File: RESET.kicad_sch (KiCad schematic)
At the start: 14 parts

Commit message: changed bus names to avoid possible conflicts, fixed unnamed busses.
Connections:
- net PABO_{2}_{3}: now reaches U?.12 (Zd)
- net PABO_{2}_{0}: now reaches U?.4 (Za)
- net PABO_{2}_{1}: now reaches U?.7 (Zb)
- net PABO_{2}_{2}: now reaches U?.9 (Zc)
- net PABO_{4}_{3}: now reaches U?.12 (Zd)
- net PABO_{4}_{0}: now reaches U?.4 (Za)
- net PABO_{4}_{1}: now reaches U?.7 (Zb)
- net PABO_{4}_{2}: now reaches U?.9 (Zc)
- net PABO_{3}_{2}: now reaches U?.12 (Zd)
- net PABO_{3}_{0}: now reaches U?.4 (Za)
- net PABO_{3}_{1}: now reaches U?.7 (Zb)
- net PABO_{3}_{3}: now reaches U?.9 (Zc)
- net PABO_{1}_{3}: now reaches U?.12 (Zd)
- net PABO_{1}_{0}: now reaches U?.4 (Za)
- net PABO_{1}_{1}: now reaches U?.7 (Zb)
- net PABO_{1}_{2}: now reaches U?.9 (Zc)
- net PABO_{4}_{7}: now reaches U?.12 (Zd)
- net PABO_{4}_{4}: now reaches U?.4 (Za)
- net PABO_{4}_{5}: now reaches U?.7 (Zb)
- net PABO_{4}_{6}: now reaches U?.9 (Zc)
- net PABO_{2}_{7}: now reaches U?.12 (Zd)
- net PABO_{2}_{4}: now reaches U?.4 (Za)
- net PABO_{2}_{5}: now reaches U?.7 (Zb)
- net PABO_{2}_{6}: now reaches U?.9 (Zc)
- net PABO_{3}_{7}: now reaches U?.12 (Zd)
- net PABO_{3}_{4}: now reaches U?.4 (Za)
- net PABO_{3}_{5}: now reaches U?.7 (Zb)
- net PABO_{3}_{6}: now reaches U?.9 (Zc)
- net PABO_{1}_{7}: now reaches U?.12 (Zd)
- net PABO_{1}_{4}: now reaches U?.4 (Za)
- net PABO_{1}_{5}: now reaches U?.7 (Zb)
- net PABO_{1}_{6}: now reaches U?.9 (Zc)
- net PANI_{1}_{0} renamed PABI_{1}_{0}
- net PANI_{1}_{1} renamed PABI_{1}_{1}
- net PANI_{1}_{2} renamed PABI_{1}_{2}
- net PANI_{1}_{3} renamed PABI_{1}_{3}
- net PANI_{1}_{4} renamed PABI_{1}_{4}
- net PANI_{1}_{5} renamed PABI_{1}_{5}
- net PANI_{1}_{6} renamed PABI_{1}_{6}
- net PANI_{1}_{7} renamed PABI_{1}_{7}
- net PANI_{2}_{0} renamed PABI_{2}_{0}
- net PANI_{2}_{1} renamed PABI_{2}_{1}
- net PANI_{2}_{2} renamed PABI_{2}_{2}
- net PANI_{2}_{3} renamed PABI_{2}_{3}
- net PANI_{2}_{4} renamed PABI_{2}_{4}
- net PANI_{2}_{5} renamed PABI_{2}_{5}
- net PANI_{2}_{6} renamed PABI_{2}_{6}
- net PANI_{2}_{7} renamed PABI_{2}_{7}
- net PANI_{3}_{0} renamed PABI_{3}_{0}
- net PANI_{3}_{1} renamed PABI_{3}_{1}
- net PANI_{3}_{2} renamed PABI_{3}_{2}
- net PANI_{3}_{3} renamed PABI_{3}_{3}
- net PANI_{3}_{4} renamed PABI_{3}_{4}
- net PANI_{3}_{5} renamed PABI_{3}_{5}
- net PANI_{3}_{6} renamed PABI_{3}_{6}
- net PANI_{3}_{7} renamed PABI_{3}_{7}
- net PANI_{4}_{0} renamed PABI_{4}_{0}
- net PANI_{4}_{1} renamed PABI_{4}_{1}
- net PANI_{4}_{2} renamed PABI_{4}_{2}
- net PANI_{4}_{3} renamed PABI_{4}_{3}
- net PANI_{4}_{4} renamed PABI_{4}_{4}
- net PANI_{4}_{5} renamed PABI_{4}_{5}
- net PANI_{4}_{6} renamed PABI_{4}_{6}
- net PANI_{4}_{7} renamed PABI_{4}_{7}

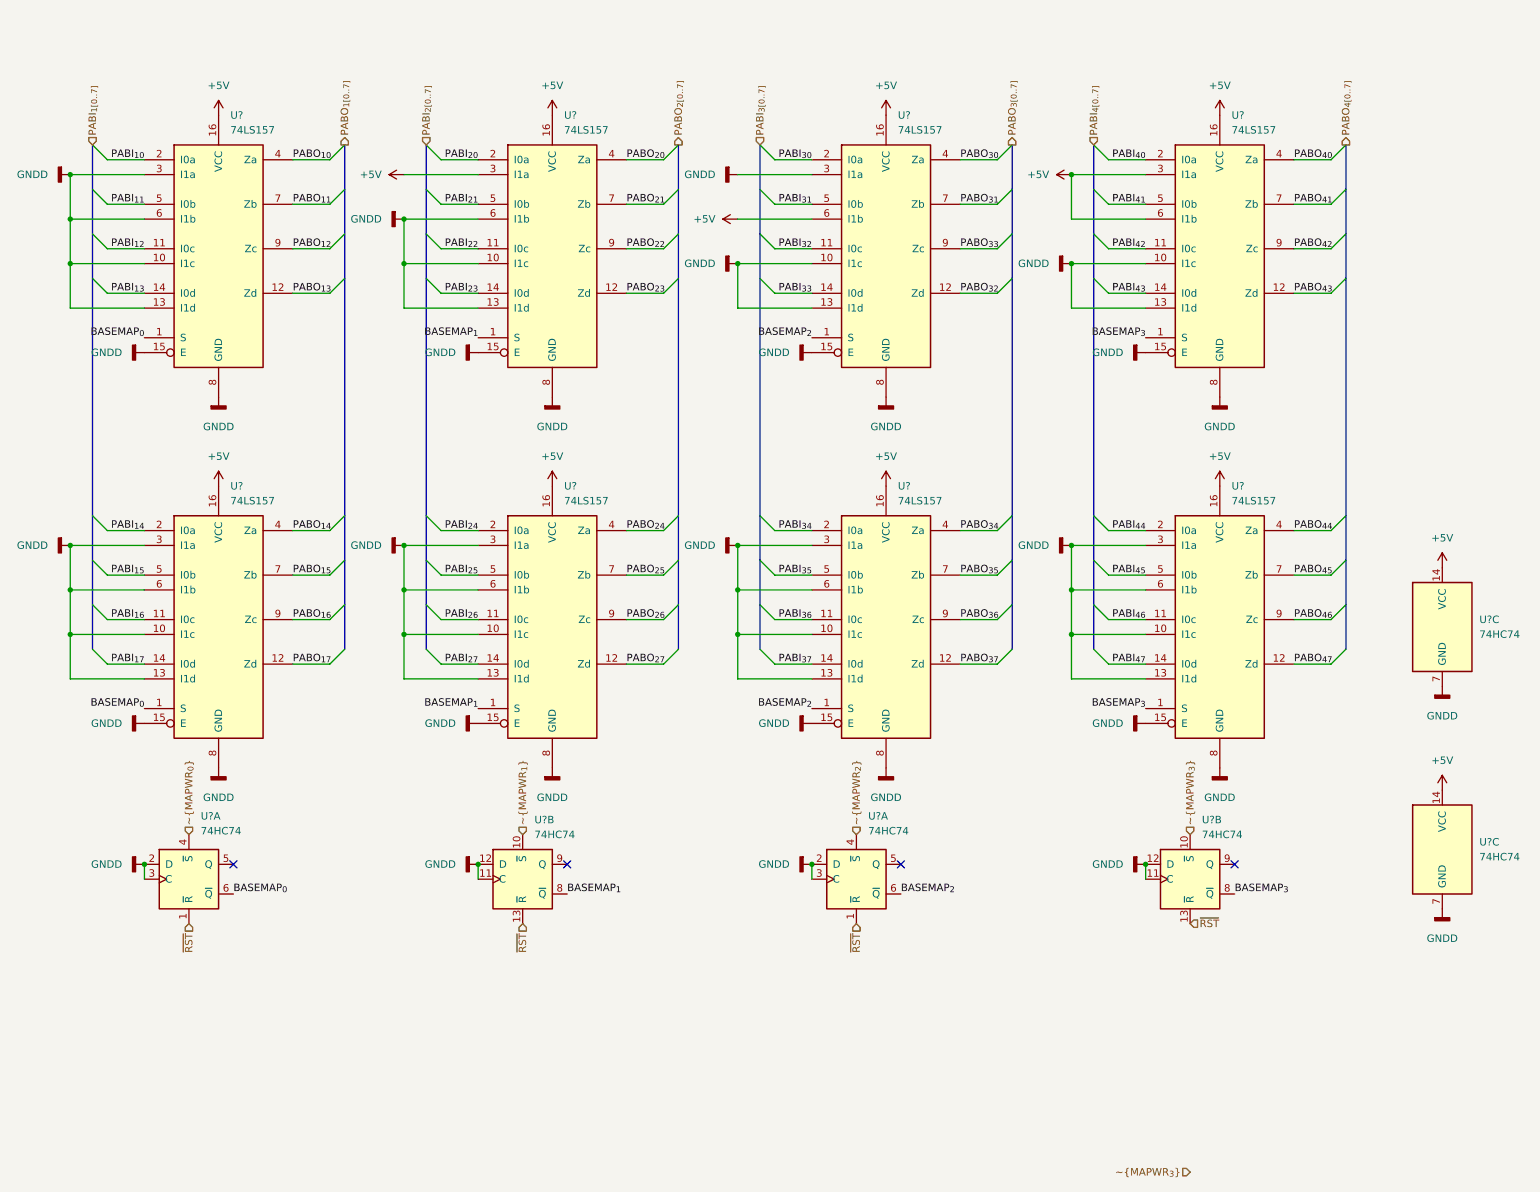
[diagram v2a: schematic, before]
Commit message: added decoupling capacitors, perhaps too many? idk better more than less!
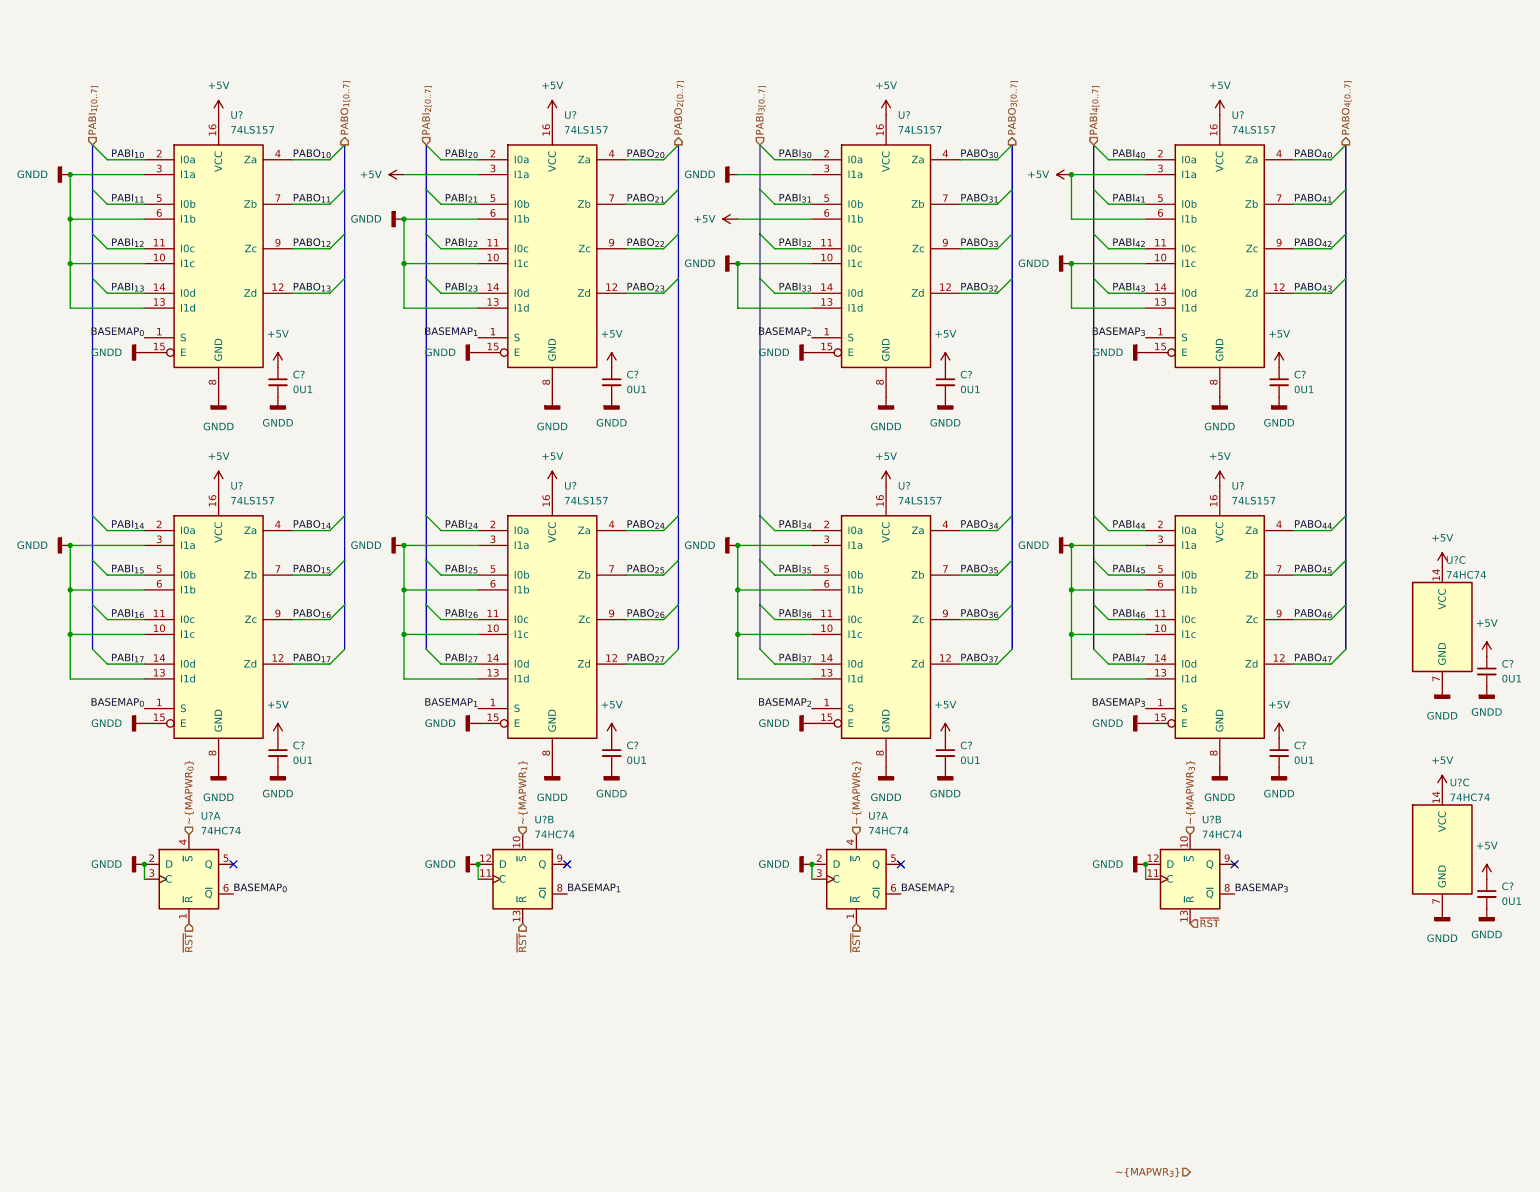
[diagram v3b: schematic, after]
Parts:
- added C? (x10): 0U1, symbol Device:C_Small
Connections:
- net +5V: now also C?.1, C?.1, C?.1, C?.1, C?.1, C?.1, C?.1, C?.1, C?.1, C?.1
- net GNDD: now also C?.2, C?.2, C?.2, C?.2, C?.2, C?.2, C?.2, C?.2, C?.2, C?.2

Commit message: some clean up and simplification, as well as some renaming
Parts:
- gave numbers to parts that had none: 20
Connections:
- net PABI_{1}_{0} renamed PABI_{1}0
- net PABI_{1}_{1} renamed PABI_{1}1
- net PABI_{1}_{2} renamed PABI_{1}2
- net PABI_{1}_{3} renamed PABI_{1}3
- net PABI_{1}_{4} renamed PABI_{1}4
- net PABI_{1}_{5} renamed PABI_{1}5
- net PABI_{1}_{6} renamed PABI_{1}6
- net PABI_{1}_{7} renamed PABI_{1}7
- net PABI_{2}_{0} renamed PABI_{2}0
- net PABI_{2}_{1} renamed PABI_{2}1
- net PABI_{2}_{2} renamed PABI_{2}2
- net PABI_{2}_{3} renamed PABI_{2}3
- net PABI_{2}_{4} renamed PABI_{2}4
- net PABI_{2}_{5} renamed PABI_{2}5
- net PABI_{2}_{6} renamed PABI_{2}6
- net PABI_{2}_{7} renamed PABI_{2}7
- net PABI_{3}_{0} renamed PABI_{3}0
- net PABI_{3}_{1} renamed PABI_{3}1
- net PABI_{3}_{2} renamed PABI_{3}2
- net PABI_{3}_{3} renamed PABI_{3}3
- net PABI_{3}_{4} renamed PABI_{3}4
- net PABI_{3}_{5} renamed PABI_{3}5
- net PABI_{3}_{6} renamed PABI_{3}6
- net PABI_{3}_{7} renamed PABI_{3}7
- net PABI_{4}_{0} renamed PABI_{4}0
- net PABI_{4}_{1} renamed PABI_{4}1
- net PABI_{4}_{2} renamed PABI_{4}2
- net PABI_{4}_{3} renamed PABI_{4}3
- net PABI_{4}_{4} renamed PABI_{4}4
- net PABI_{4}_{5} renamed PABI_{4}5
- net PABI_{4}_{6} renamed PABI_{4}6
- net PABI_{4}_{7} renamed PABI_{4}7
- net PABO_{1}_{0} renamed PABO_{1}0
- net PABO_{1}_{1} renamed PABO_{1}1
- net PABO_{1}_{2} renamed PABO_{1}2
- net PABO_{1}_{3} renamed PABO_{1}3
- net PABO_{1}_{4} renamed PABO_{1}4
- net PABO_{1}_{5} renamed PABO_{1}5
- net PABO_{1}_{6} renamed PABO_{1}6
- net PABO_{1}_{7} renamed PABO_{1}7
- net PABO_{2}_{0} renamed PABO_{2}0
- net PABO_{2}_{1} renamed PABO_{2}1
- net PABO_{2}_{2} renamed PABO_{2}2
- net PABO_{2}_{3} renamed PABO_{2}3
- net PABO_{2}_{4} renamed PABO_{2}4
- net PABO_{2}_{5} renamed PABO_{2}5
- net PABO_{2}_{6} renamed PABO_{2}6
- net PABO_{2}_{7} renamed PABO_{2}7
- net PABO_{3}_{0} renamed PABO_{3}0
- net PABO_{3}_{1} renamed PABO_{3}1
- net PABO_{3}_{2} renamed PABO_{3}2
- net PABO_{3}_{3} renamed PABO_{3}3
- net PABO_{3}_{4} renamed PABO_{3}4
- net PABO_{3}_{5} renamed PABO_{3}5
- net PABO_{3}_{6} renamed PABO_{3}6
- net PABO_{3}_{7} renamed PABO_{3}7
- net PABO_{4}_{0} renamed PABO_{4}0
- net PABO_{4}_{1} renamed PABO_{4}1
- net PABO_{4}_{2} renamed PABO_{4}2
- net PABO_{4}_{3} renamed PABO_{4}3
- net PABO_{4}_{4} renamed PABO_{4}4
- net PABO_{4}_{5} renamed PABO_{4}5
- net PABO_{4}_{6} renamed PABO_{4}6
- net PABO_{4}_{7} renamed PABO_{4}7

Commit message: begin integration of logic into atf1508
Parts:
- C23, C24, C25, C26, C27, C28, C29, C30, C31, C32: footprint (none) -> Capacitor_SMD:C_0603_1608Metric
- U49, U54: footprint (none) -> Package_SO:TSSOP-14_4.4x5mm_P0.65mm
- U50, U51, U52, U53, U55, U56, U57, U58: footprint (none) -> Package_SO:TSSOP-16_4.4x5mm_P0.65mm
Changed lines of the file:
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@@
       (effects (font (size 1.27 1.27)) (justify left))
     )
-    (property "Footprint" "" (id 2) (at 181.61 133.35 0)
+    (property "Footprint" "Capacitor_SMD:C_0603_1608Metric" (id 2) (at 181.61 133.35 0)
       (effects (font (size 1.27 1.27)) hide)
     )
@@
       (effects (font (size 1.27 1.27)) (justify left))
     )
-    (property "Footprint" "" (id 2) (at 114.3 46.99 0)
+    (property "Footprint" "Package_SO:TSSOP-16_4.4x5mm_P0.65mm" (id 2) (at 114.3 46.99 0)
       (effects (font (size 1.27 1.27)) hide)
     )
@@
       (effects (font (size 1.27 1.27)) (justify left))
     )
-    (property "Footprint" "" (id 2) (at 228.6 46.99 0)
+    (property "Footprint" "Package_SO:TSSOP-16_4.4x5mm_P0.65mm" (id 2) (at 228.6 46.99 0)
       (effects (font (size 1.27 1.27)) hide)
     )
@@
       (effects (font (size 1.27 1.27)) (justify left))
     )
-    (property "Footprint" "" (id 2) (at 274.32 119.38 0)
+    (property "Footprint" "Capacitor_SMD:C_0603_1608Metric" (id 2) (at 274.32 119.38 0)
       (effects (font (size 1.27 1.27)) hide)
     )
@@
       (effects (font (size 1.27 1.27)) (justify left))
     )
-    (property "Footprint" "" (id 2) (at 52.07 154.94 0)
+    (property "Footprint" "Package_SO:TSSOP-14_4.4x5mm_P0.65mm" (id 2) (at 52.07 154.94 0)
       (effects (font (size 1.27 1.27)) hide)
     )
@@
       (effects (font (size 1.27 1.27)) (justify left))
     )
-    (property "Footprint" "" (id 2) (at 109.22 154.94 0)
+    (property "Footprint" "Package_SO:TSSOP-14_4.4x5mm_P0.65mm" (id 2) (at 109.22 154.94 0)
       (effects (font (size 1.27 1.27)) hide)
     )
@@
       (effects (font (size 1.27 1.27)) (justify left))
     )
-    (property "Footprint" "" (id 2) (at 171.45 46.99 0)
+    (property "Footprint" "Package_SO:TSSOP-16_4.4x5mm_P0.65mm" (id 2) (at 171.45 46.99 0)
       (effects (font (size 1.27 1.27)) hide)
     )
@@
       (effects (font (size 1.27 1.27)) (justify left))
     )
-    (property "Footprint" "" (id 2) (at 57.15 46.99 0)
+    (property "Footprint" "Package_SO:TSSOP-16_4.4x5mm_P0.65mm" (id 2) (at 57.15 46.99 0)
       (effects (font (size 1.27 1.27)) hide)
     )
@@
       (effects (font (size 1.27 1.27)) (justify left))
     )
-    (property "Footprint" "" (id 2) (at 238.76 133.35 0)
+    (property "Footprint" "Capacitor_SMD:C_0603_1608Metric" (id 2) (at 238.76 133.35 0)
       (effects (font (size 1.27 1.27)) hide)
     )
@@
       (effects (font (size 1.27 1.27)) (justify left))
     )
-    (property "Footprint" "" (id 2) (at 124.46 69.85 0)
+    (property "Footprint" "Capacitor_SMD:C_0603_1608Metric" (id 2) (at 124.46 69.85 0)
       (effects (font (size 1.27 1.27)) hide)
     )
@@
       (effects (font (size 1.27 1.27)) (justify left))
     )
-    (property "Footprint" "" (id 2) (at 67.31 133.35 0)
+    (property "Footprint" "Capacitor_SMD:C_0603_1608Metric" (id 2) (at 67.31 133.35 0)
       (effects (font (size 1.27 1.27)) hide)
     )
@@
       (effects (font (size 1.27 1.27)) (justify left))
     )
-    (property "Footprint" "" (id 2) (at 228.6 110.49 0)
+    (property "Footprint" "Package_SO:TSSOP-16_4.4x5mm_P0.65mm" (id 2) (at 228.6 110.49 0)
       (effects (font (size 1.27 1.27)) hide)
     )
@@
       (effects (font (size 1.27 1.27)) (justify left))
     )
-    (property "Footprint" "" (id 2) (at 114.3 110.49 0)
+    (property "Footprint" "Package_SO:TSSOP-16_4.4x5mm_P0.65mm" (id 2) (at 114.3 110.49 0)
       (effects (font (size 1.27 1.27)) hide)
     )
@@
       (effects (font (size 1.27 1.27)) (justify left))
     )
-    (property "Footprint" "" (id 2) (at 171.45 110.49 0)
+    (property "Footprint" "Package_SO:TSSOP-16_4.4x5mm_P0.65mm" (id 2) (at 171.45 110.49 0)
       (effects (font (size 1.27 1.27)) hide)
     )
@@
       (effects (font (size 1.27 1.27)) (justify left))
     )
-    (property "Footprint" "" (id 2) (at 124.46 133.35 0)
+    (property "Footprint" "Capacitor_SMD:C_0603_1608Metric" (id 2) (at 124.46 133.35 0)
       (effects (font (size 1.27 1.27)) hide)
     )
@@
       (effects (font (size 1.27 1.27)) (justify left))
     )
-    (property "Footprint" "" (id 2) (at 223.52 154.94 0)
+    (property "Footprint" "Package_SO:TSSOP-14_4.4x5mm_P0.65mm" (id 2) (at 223.52 154.94 0)
       (effects (font (size 1.27 1.27)) hide)
     )
@@
       (effects (font (size 1.27 1.27)) (justify left))
     )
-    (property "Footprint" "" (id 2) (at 166.37 154.94 0)
+    (property "Footprint" "Package_SO:TSSOP-14_4.4x5mm_P0.65mm" (id 2) (at 166.37 154.94 0)
       (effects (font (size 1.27 1.27)) hide)
     )
@@
       (effects (font (size 1.27 1.27)) (justify left))
     )
-    (property "Footprint" "" (id 2) (at 266.7 111.76 0)
+    (property "Footprint" "Package_SO:TSSOP-14_4.4x5mm_P0.65mm" (id 2) (at 266.7 111.76 0)
       (effects (font (size 1.27 1.27)) hide)
     )
@@
       (effects (font (size 1.27 1.27)) (justify left))
     )
-    (property "Footprint" "" (id 2) (at 274.32 157.48 0)
+    (property "Footprint" "Capacitor_SMD:C_0603_1608Metric" (id 2) (at 274.32 157.48 0)
       (effects (font (size 1.27 1.27)) hide)
     )
@@
       (effects (font (size 1.27 1.27)) (justify left))
     )
-    (property "Footprint" "" (id 2) (at 57.15 110.49 0)
+    (property "Footprint" "Package_SO:TSSOP-16_4.4x5mm_P0.65mm" (id 2) (at 57.15 110.49 0)
       (effects (font (size 1.27 1.27)) hide)
     )
@@
       (effects (font (size 1.27 1.27)) (justify left))
     )
-    (property "Footprint" "" (id 2) (at 67.31 69.85 0)
+    (property "Footprint" "Capacitor_SMD:C_0603_1608Metric" (id 2) (at 67.31 69.85 0)
       (effects (font (size 1.27 1.27)) hide)
     )
@@
       (effects (font (size 1.27 1.27)) (justify left))
     )
-    (property "Footprint" "" (id 2) (at 238.76 69.85 0)
+    (property "Footprint" "Capacitor_SMD:C_0603_1608Metric" (id 2) (at 238.76 69.85 0)
       (effects (font (size 1.27 1.27)) hide)
     )
@@
       (effects (font (size 1.27 1.27)) (justify left))
     )
-    (property "Footprint" "" (id 2) (at 181.61 69.85 0)
+    (property "Footprint" "Capacitor_SMD:C_0603_1608Metric" (id 2) (at 181.61 69.85 0)
       (effects (font (size 1.27 1.27)) hide)
     )
@@
       (effects (font (size 1.27 1.27)) (justify left))
     )
-    (property "Footprint" "" (id 2) (at 266.7 149.86 0)
-      (effects (font (size 1.27 1.27)) hide)
-    )
+    (property "Footprint" "Package_SO:TSSOP-14_4.4x5mm_P0.65mm" (id 2) (at 266.7 149.86 0)
+      (effects (font (size 1.27 1.27)) hide)
+    )
